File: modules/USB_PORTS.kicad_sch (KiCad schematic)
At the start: 10 parts, among them J6 USB_C_Receptacle, Q1 AO3401A, SW5 SW, U10 USBLC6-2SC6

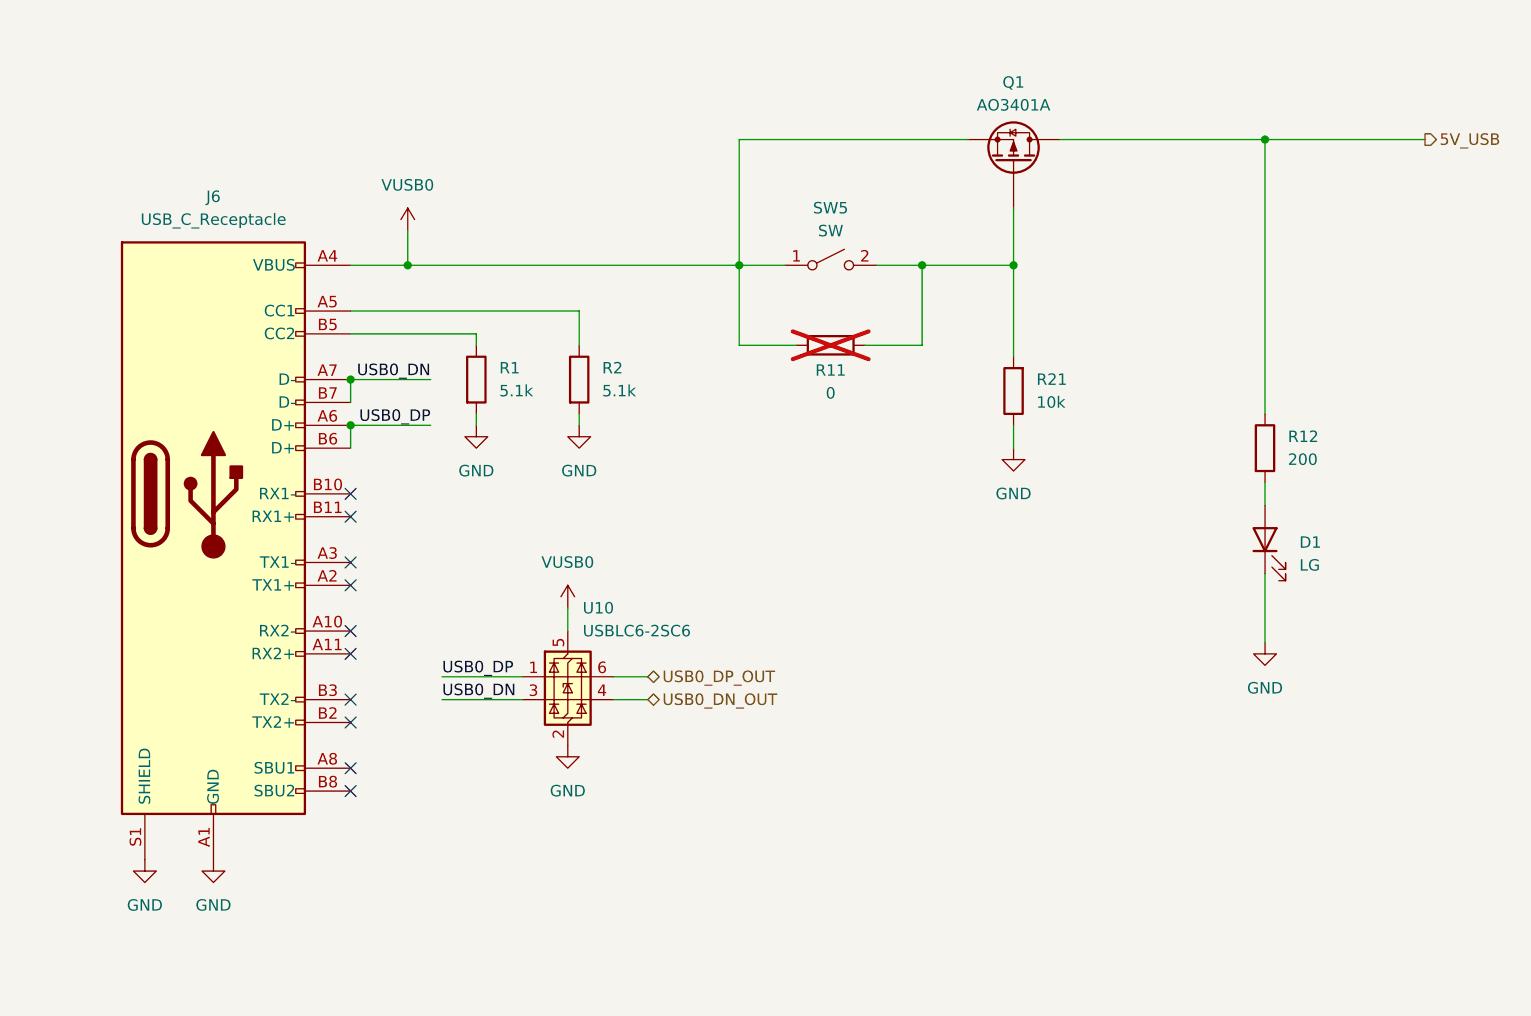
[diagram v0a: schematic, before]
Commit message: correction of mikroBUS, USB on ESP32 and power mosfet
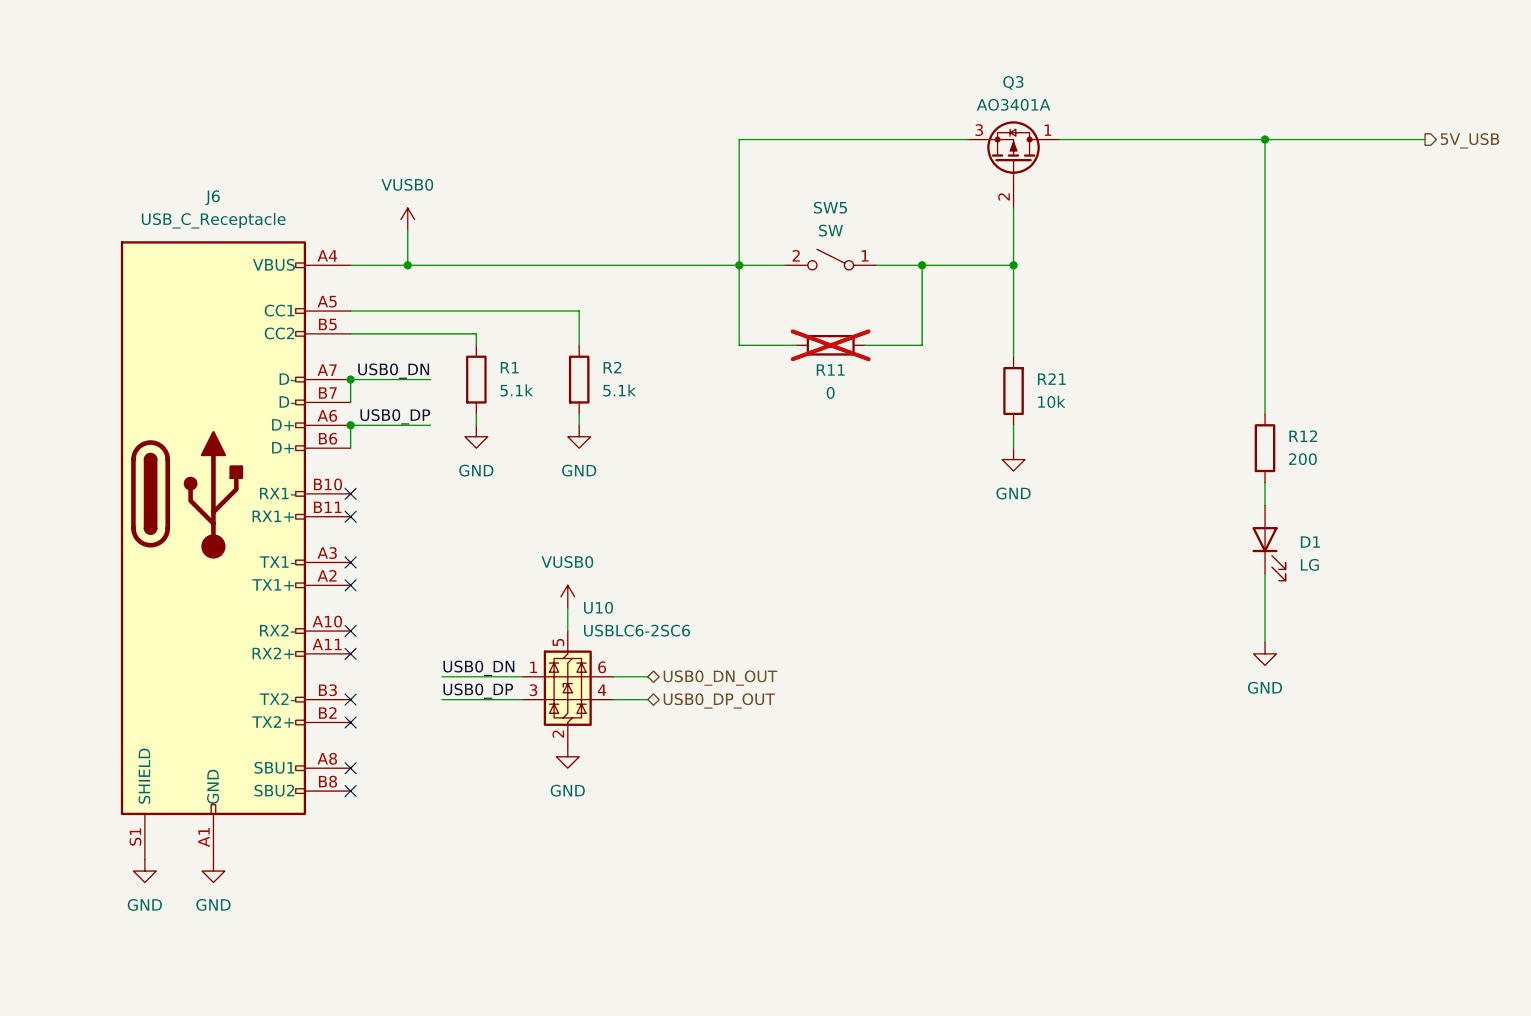
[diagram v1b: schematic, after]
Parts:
- removed Q1: AO3401A, Package_TO_SOT_SMD:SOT-23, symbol Device:Q_PMOS
- added Q3: AO3401A, Package_TO_SOT_SMD:SOT-23, symbol Transistor_FET:Q_PMOS_DGS
- J6: footprint Connector_USB:USB_C_Receptacle_Amphenol_12401610E4-2A -> Connector_USB:USB_C_Receptacle_GCT_USB4105-xx-A_16P_TopMnt_Horizontal; Part Number 12401610E4#2A -> USB4105-GF-A-120
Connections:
- net 5V_USB: now also Q3.1 (D)
- net USB0_DN: now also U10.1 (I/O1); no longer U10.3 (I/O2)
- net USB0_DN_OUT: now also U10.6 (I/O1); no longer U10.4 (I/O2)
- net USB0_DP: now also U10.3 (I/O2); no longer U10.1 (I/O1)
- net USB0_DP_OUT: now also U10.4 (I/O2); no longer U10.6 (I/O1)
- net VUSB0: now also SW5.2 (B), Q3.3 (S); no longer SW5.1 (A)
- net at R11.2, R21.2: now also SW5.1 (A), Q3.2 (G); no longer SW5.2 (B)
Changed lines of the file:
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@@
+		)
+	)
+	(label "USB0_DP"
+		(at 127 114.3 0)
+		(effects
+			(font
+				(size 1.27 1.27)
+			)
+			(justify left bottom)
+		)
+	)
+	(label "USB0_DN"
+		(at 127 111.76 0)
+		(effects
+			(font
+				(size 1.27 1.27)
+			)
+			(justify left bottom)
 		)
 	)
@@
 		)
 	)
-	(label "USB0_DP"
-		(at 127 111.76 0)
-		(effects
-			(font
-				(size 1.27 1.27)
-			)
-			(justify left bottom)
-		)
-	)
-	(label "USB0_DN"
-		(at 127 114.3 0)
-		(effects
-			(font
-				(size 1.27 1.27)
-			)
-			(justify left bottom)
-		)
-	)
-	(hierarchical_label "USB0_DP_OUT"
+	(hierarchical_label "USB0_DN_OUT"
 		(shape bidirectional)
 		(at 149.86 111.76 0)
@@
 		)
 	)
-	(hierarchical_label "USB0_DN_OUT"
+	(hierarchical_label "USB0_DP_OUT"
 		(shape bidirectional)
 		(at 149.86 114.3 0)
@@
 		(lib_id "Switch:SW_SPST")
 		(at 170.18 66.04 0)
-		(unit 1)
-		(exclude_from_sim no)
-		(in_bom yes)
-		(on_board yes)
-		(dnp no)
-		(fields_autoplaced yes)
+		(mirror y)
+		(unit 1)
+		(exclude_from_sim no)
+		(in_bom yes)
+		(on_board yes)
+		(dnp no)
 		(property "Reference" "SW5"
 			(at 170.18 59.69 0)
@@
 			)
 		)
-		(property "Footprint" "Connector_USB:USB_C_Receptacle_Amphenol_12401610E4-2A"
+		(property "Footprint" "Connector_USB:USB_C_Receptacle_GCT_USB4105-xx-A_16P_TopMnt_Horizontal"
 			(at 105.41 91.44 0)
 			(effects
@@
 			)
 		)
-		(property "Description" "CONN RCP USB3.1 TYPEC 24P SMD RA"
+		(property "Description" "https://gct.co/files/specs/usb4105-spec.pdf"
 			(at 101.6 91.44 0)
 			(effects
@@
 			)
 		)
-		(property "Part Number" "12401610E4#2A"
+		(property "Part Number" "USB4105-GF-A-120"
 			(at 101.6 91.44 0)
 			(effects
@@
 	)
 	(symbol
+		(lib_id "Transistor_FET:Q_PMOS_DGS")
+		(at 190.5 54.61 270)
+		(mirror x)
+		(unit 1)
+		(exclude_from_sim no)
+		(in_bom yes)
+		(on_board yes)
+		(dnp no)
+		(property "Reference" "Q3"
+			(at 190.5 45.72 90)
+			(effects
+				(font
+					(size 1.27 1.27)
+				)
+			)
+		)
+		(property "Value" "AO3401A"
+			(at 190.5 48.26 90)
+			(effects
+				(font
+					(size 1.27 1.27)
+				)
+			)
+		)
+		(property "Footprint" "Package_TO_SOT_SMD:SOT-23"
+			(at 193.04 49.53 0)
+			(effects
+				(font
+					(size 1.27 1.27)
+				)
+				(hide yes)
+			)
+		)
+		(property "Datasheet" "https://aosmd.com/sites/default/files/res/datasheets/AO3401A.pdf"
+			(at 190.5 54.61 0)
+			(effects
+				(font
+					(size 1.27 1.27)
+				)
+				(hide yes)
+			)
+		)
+		(property "Description" "MOSFET P-CH 30V 4A SOT23-3L"
+			(at 190.5 54.61 0)
+			(effects
+				(font
+					(size 1.27 1.27)
+				)
+				(hide yes)
+			)
+		)
+		(property "Part Number" "AO3401A"
+			(at 190.5 54.61 90)
+			(effects
+				(font
+					(size 1.27 1.27)
+				)
+				(hide yes)
+			)
+		)
+		(property "Provider" "Digikey"
+			(at 190.5 54.61 90)
+			(effects
+				(font
+					(size 1.27 1.27)
+				)
+				(hide yes)
+			)
+		)
+		(pin "2"
+		)
+		(pin "3"
+		)
+		(pin "1"
+		)
+		(instances
+			(project ""
+				(path "/3efb3214-cf20-4475-a403-c426a77bfef6/3930103f-b854-406a-9821-18948625639a"
+					(reference "Q3")
+					(unit 1)
+				)
+			)
+		)
+	)
+	(symbol
 		(lib_id "power:+3V3")
 		(at 123.19 62.23 0)
@@
 					(unit 1)
 				)
-			)
-		)
-	)
-	(symbol
-		(lib_id "Device:Q_PMOS")
-		(at 190.5 54.61 270)
-		(mirror x)
-		(unit 1)
-		(exclude_from_sim no)
-		(in_bom yes)
-		(on_board yes)
-		(dnp no)
-		(property "Reference" "Q1"
-			(at 190.5 45.72 90)
-			(effects
-				(font
-					(size 1.27 1.27)
-				)
-			)
-		)
-		(property "Value" "AO3401A"
-			(at 190.5 48.26 90)
-			(effects
-				(font
-					(size 1.27 1.27)
-				)
-			)
-		)
-		(property "Footprint" "Package_TO_SOT_SMD:SOT-23"
-			(at 193.04 49.53 0)
-			(effects
-				(font
-					(size 1.27 1.27)
-				)
-				(hide yes)
-			)
-		)
-		(property "Datasheet" "https://aosmd.com/sites/default/files/res/datasheets/AO3401A.pdf"
-			(at 190.5 54.61 0)
-			(effects
-				(font
-					(size 1.27 1.27)
-				)
-				(hide yes)
-			)
-		)
-		(property "Description" "MOSFET P-CH 30V 4A SOT23-3L"
-			(at 190.5 54.61 0)
-			(effects
-				(font
-					(size 1.27 1.27)
-				)
-				(hide yes)
-			)
-		)
-		(property "Part Number" "AO3401A"
-			(at 190.5 54.61 90)
-			(effects
-				(font
-					(size 1.27 1.27)
-				)
-				(hide yes)
-			)
-		)
-		(property "Provider" "Digikey"
-			(at 190.5 54.61 90)
-			(effects
-				(font
-					(size 1.27 1.27)
-				)
-				(hide yes)
-			)
-		)
-		(pin "G"
-		)
-		(pin "D"
-		)
-		(pin "S"
-		)
-		(instances
-			(project "RP_devBoard"
-				(path "/3efb3214-cf20-4475-a403-c426a77bfef6/3930103f-b854-406a-9821-18948625639a"
-					(reference "Q1")
-					(unit 1)
-				)

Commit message: save
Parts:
- added TP1, TP2: TestPoint, Connector_Pin:Pin_D1.0mm_L10.0mm, symbol Connector:TestPoint
- added TP3, TP7, TP8: TestPoint, TestPoint:TestPoint_THTPad_D1.0mm_Drill0.5mm, symbol Connector:TestPoint
- D1: footprint Inductor_SMD:L_0603_1608Metric -> LED_SMD:LED_0805_2012Metric
- R11: footprint Resistor_SMD:R_0603_1608Metric -> Resistor_SMD:R_0805_2012Metric
- SW5: footprint Button_Switch_SMD:SW_DPDT_CK_JS202011JCQN -> Button_Switch_SMD:SW_DIP_SPSTx01_Slide_6.7x4.1mm_W6.73mm_P2.54mm_LowProfile_JPin
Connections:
- net 5V_USB: now also TP3.1
- net GND: now also TP1.1
- net USB0_DN_OUT: now also TP8.1
- net USB0_DP_OUT: now also TP7.1
- net VUSB0: now also TP2.1
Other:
- moved on the sheet: U10

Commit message: Cambio de layout, correccion de pinout
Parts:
- removed TP1: TestPoint, Connector_Pin:Pin_D1.0mm_L10.0mm, symbol Connector:TestPoint
- added TP2: TestPoint, Sadman_TP:TP_2.8mm_1mm, symbol Connector:TestPoint
- TP1: renamed from TP2; footprint Connector_Pin:Pin_D1.0mm_L10.0mm -> Sadman_TP:TP_2.8mm_1mm
- TP3, TP7, TP8: footprint TestPoint:TestPoint_THTPad_D1.0mm_Drill0.5mm -> Sadman_TP:TP_2.8mm_1mm
- renumbered Q3 to Q1, R21 to R10, R12 to R11, R11 to R9, SW5 to SW2, U10 to U3
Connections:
- net 5V_USB: now also TP7.1; no longer TP3.1
- net GND: now also TP3.1
- net USB0_DN_OUT: now also TP2.1; no longer TP8.1
- net USB0_DP_OUT: now also TP8.1; no longer TP7.1
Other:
- moved on the sheet: D1, J6, Q1, R1, R10, R11, R2, R9, SW2, TP1, U3

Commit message: finishing version 1.0
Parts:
- D1: Part Number 150060VS55040 -> LG R971-KN-1-0-20-R18
- R9: now left out of the parts list
- SW2: value SW -> A6SN; Part Number JS202011SCQN -> A6SN-1101
